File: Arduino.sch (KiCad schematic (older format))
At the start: 0 parts

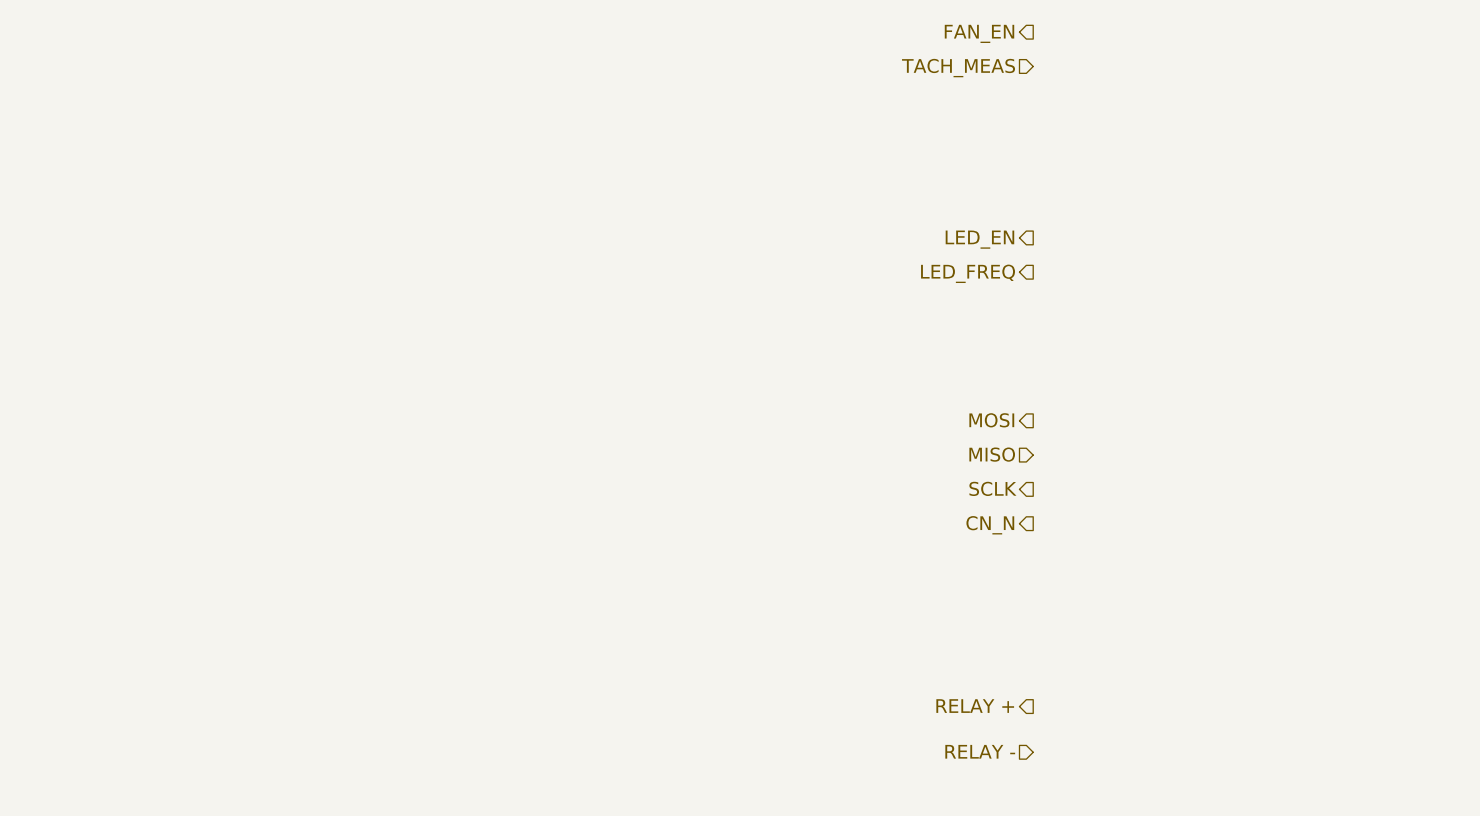
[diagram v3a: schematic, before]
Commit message: Completed Arduino Block Diagram and Fan Redesign
The commits as of this are now up to date with the videos released for
Contextual Electronics, Week 3.
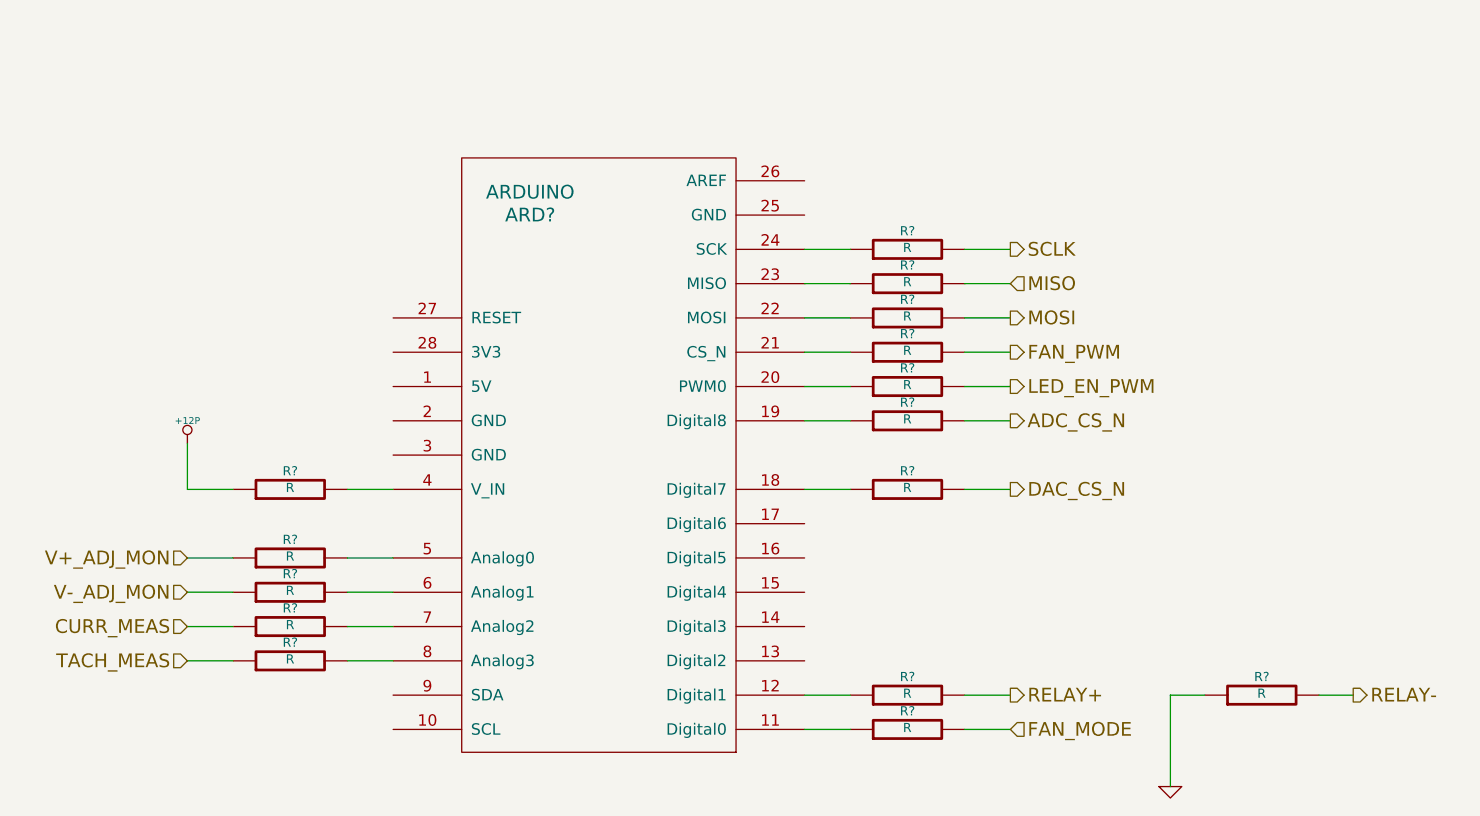
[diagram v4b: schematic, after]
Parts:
- added ARD?: ARDUINO, ~, symbol ARDUINO
- added R? (x15): R, ~, symbol R
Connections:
- net MISO: now also R?.2
- net MOSI: now also R?.2
- net SCLK: now also R?.2
- net TACH_MEAS: now also R?.1
- new net: ARD?.11 (Digital0), R?.1
- new net: ARD?.12 (Digital1), R?.1
- new net: ARD?.18 (Digital7), R?.1
- new net: ARD?.19 (Digital8), R?.1
- new net: ARD?.20 (PWM0), R?.1
- new net: ARD?.21 (CS_N), R?.1
- new net: ARD?.22 (MOSI), R?.1
- new net: ARD?.23 (MISO), R?.1
- new net: ARD?.24 (SCK), R?.1
- new net: ARD?.4 (V_IN), R?.2
- new net: ARD?.5 (Analog0), R?.2
- new net: ARD?.6 (Analog1), R?.2
- new net: ARD?.7 (Analog2), R?.2
- new net: ARD?.8 (Analog3), R?.2
- new net +12P: R?.1
- new net ADC_CS_N: R?.2
- new net CURR_MEAS: R?.1
- new net DAC_CS_N: R?.2
- new net FAN_MODE: R?.2
- new net FAN_PWM: R?.2
- new net GND: R?.1
- new net LED_EN_PWM: R?.2
- new net RELAY+: R?.2
- new net RELAY-: R?.2
- new net V+_ADJ_MON: R?.1
- new net V-_ADJ_MON: R?.1

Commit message: Initial layout of relay and thermocouple
All block diagrams completed through Week 3.  Component selection
spreadsheets created: Bench Buddy Session 1CE.xlsx = official part
selection and bom.xlsx is the version I came up with.

Part association and initial layout of the Relay and Thermocouple
sections completed.
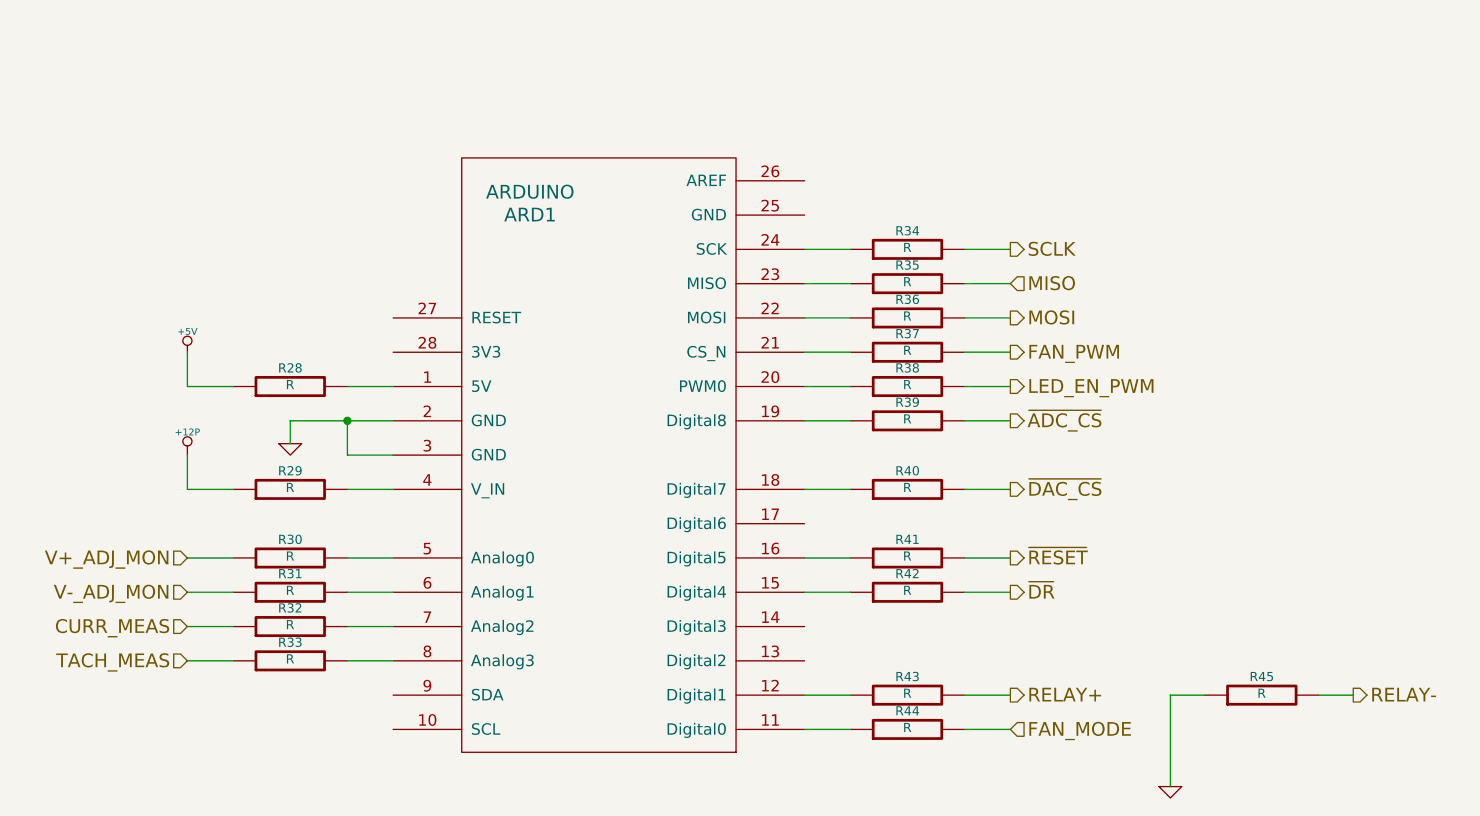
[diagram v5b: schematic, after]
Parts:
- added R28, R41, R42: R, ~, symbol R
- gave numbers to parts that had none: 16
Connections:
- net GND: now also ARD1.2 (GND), ARD1.3 (GND)
- net at ARD1.1 (5V): now also R28.2
- net at ARD1.15 (Digital4): now also R42.1
- net at ARD1.16 (Digital5): now also R41.1
- net ADC_CS_N renamed ~ADC_CS
- net DAC_CS_N renamed ~DAC_CS
- new net +5V: R28.1
- new net ~DR: R42.2
- new net ~RESET: R41.2
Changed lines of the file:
@@
 Sheet 9 9
 Title ""
-Date "6 feb 2014"
+Date "21 feb 2014"
 Rev ""
 Comp ""
@@
 SCLK
 Text HLabel 7900 4300 2    60   Output ~ 0
-DAC_CS_N
+~DAC_CS
 Text HLabel 7900 3850 2    60   Output ~ 0
 LED_EN_PWM
@@
 TACH_MEAS
 $Comp
-L ARDUINO ARD?
+L ARDUINO ARD1
 U 1 1 52F3CC17
 P 6100 4150
-F 0 "ARD?" H 5800 5200 60  0000 C CNN
+F 0 "ARD1" H 5800 5200 60  0000 C CNN
 F 1 "ARDUINO" H 5800 5300 60  0000 C CNN
 F 2 "~" H 6150 3600 60  0000 C CNN
@@
 	5200 4900 5000 4900
 $Comp
-L R R?
+L R R37
 U 1 1 52F3EA88
 P 7450 3700
-F 0 "R?" V 7530 3700 40  0000 C CNN
+F 0 "R37" V 7530 3700 40  0000 C CNN
 F 1 "R" V 7457 3701 40  0000 C CNN
 F 2 "~" V 7380 3700 30  0000 C CNN
@@
 	7700 3700 7900 3700
 $Comp
-L R R?
+L R R43
 U 1 1 52F3EAA6
 P 7450 5200
-F 0 "R?" V 7530 5200 40  0000 C CNN
+F 0 "R43" V 7530 5200 40  0000 C CNN
 F 1 "R" V 7457 5201 40  0000 C CNN
 F 2 "~" V 7380 5200 30  0000 C CNN
@@
 	7200 5200 7000 5200
 $Comp
-L GND #PWR?
+L GND #PWR056
 U 1 1 52F3F486
 P 8600 5600
-F 0 "#PWR?" H 8600 5600 30  0001 C CNN
+F 0 "#PWR056" H 8600 5600 30  0001 C CNN
 F 1 "GND" H 8600 5530 30  0001 C CNN
 F 2 "" H 8600 5600 60  0000 C CNN
@@
 	7900 5200 7700 5200
 $Comp
-L R R?
+L R R33
 U 1 1 52F3F4AB
 P 4750 5050
-F 0 "R?" V 4830 5050 40  0000 C CNN
+F 0 "R33" V 4830 5050 40  0000 C CNN
 F 1 "R" V 4757 5051 40  0000 C CNN
 F 2 "~" V 4680 5050 30  0000 C CNN
@@
 $EndComp
 $Comp
-L R R?
+L R R32
 U 1 1 52F3F4BB
 P 4750 4900
-F 0 "R?" V 4830 4900 40  0000 C CNN
+F 0 "R32" V 4830 4900 40  0000 C CNN
 F 1 "R" V 4757 4901 40  0000 C CNN
 F 2 "~" V 4680 4900 30  0000 C CNN
@@
 V-_ADJ_MON
 $Comp
-L R R?
+L R R31
 U 1 1 52F3F4E4
 P 4750 4750
-F 0 "R?" V 4830 4750 40  0000 C CNN
+F 0 "R31" V 4830 4750 40  0000 C CNN
 F 1 "R" V 4757 4751 40  0000 C CNN
 F 2 "~" V 4680 4750 30  0000 C CNN
@@
 $EndComp
 $Comp
-L R R?
+L R R30
 U 1 1 52F3F4EA
 P 4750 4600
-F 0 "R?" V 4830 4600 40  0000 C CNN
+F 0 "R30" V 4830 4600 40  0000 C CNN
 F 1 "R" V 4757 4601 40  0000 C CNN
 F 2 "~" V 4680 4600 30  0000 C CNN
@@
 	5200 4750 5000 4750
 $Comp
-L R R?
+L R R40
 U 1 1 52F3F532
 P 7450 4300
-F 0 "R?" V 7530 4300 40  0000 C CNN
+F 0 "R40" V 7530 4300 40  0000 C CNN
 F 1 "R" V 7457 4301 40  0000 C CNN
 F 2 "~" V 7380 4300 30  0000 C CNN
@@
 $EndComp
 $Comp
-L R R?
+L R R36
 U 1 1 52F3F538
 P 7450 3550
-F 0 "R?" V 7530 3550 40  0000 C CNN
+F 0 "R36" V 7530 3550 40  0000 C CNN
 F 1 "R" V 7457 3551 40  0000 C CNN
 F 2 "~" V 7380 3550 30  0000 C CNN
@@
 $EndComp
 $Comp
-L R R?
+L R R35
 U 1 1 52F3F53E
 P 7450 3400
-F 0 "R?" V 7530 3400 40  0000 C CNN
+F 0 "R35" V 7530 3400 40  0000 C CNN
 F 1 "R" V 7457 3401 40  0000 C CNN
 F 2 "~" V 7380 3400 30  0000 C CNN
@@
 $EndComp
 $Comp
-L R R?
+L R R34
 U 1 1 52F3F544
 P 7450 3250
-F 0 "R?" V 7530 3250 40  0000 C CNN
+F 0 "R34" V 7530 3250 40  0000 C CNN
 F 1 "R" V 7457 3251 40  0000 C CNN
 F 2 "~" V 7380 3250 30  0000 C CNN
@@
 	7200 4300 7000 4300
 $Comp
-L R R?
+L R R45
 U 1 1 52F3F59C
 P 9000 5200
-F 0 "R?" V 9080 5200 40  0000 C CNN
+F 0 "R45" V 9080 5200 40  0000 C CNN
 F 1 "R" V 9007 5201 40  0000 C CNN
 F 2 "~" V 8930 5200 30  0000 C CNN
@@
 	7700 3850 7900 3850
 $Comp
-L R R?
+L R R38
 U 1 1 52F3F5E7
 P 7450 3850
-F 0 "R?" V 7530 3850 40  0000 C CNN
+F 0 "R38" V 7530 3850 40  0000 C CNN
 F 1 "R" V 7457 3851 40  0000 C CNN
 F 2 "~" V 7380 3850 30  0000 C CNN
@@
 	7200 3850 7000 3850
 Text HLabel 7900 4000 2    60   Output ~ 0
-ADC_CS_N
+~ADC_CS
 Wire Wire Line
 	7700 4000 7900 4000
 $Comp
-L R R?
+L R R39
 U 1 1 52F47FE6
 P 7450 4000
-F 0 "R?" V 7530 4000 40  0000 C CNN
+F 0 "R39" V 7530 4000 40  0000 C CNN
 F 1 "R" V 7457 4001 40  0000 C CNN
 F 2 "~" V 7380 4000 30  0000 C CNN
@@
 	7700 5350 7900 5350
 $Comp
-L R R?
+L R R44
 U 1 1 52F41957
 P 7450 5350
-F 0 "R?" V 7530 5350 40  0000 C CNN
+F 0 "R44" V 7530 5350 40  0000 C CNN
 F 1 "R" V 7457 5351 40  0000 C CNN
 F 2 "~" V 7380 5350 30  0000 C CNN
@@
 	7200 5350 7000 5350
 $Comp
-L R R?
+L R R29
 U 1 1 52F42414
 P 4750 4300
-F 0 "R?" V 4830 4300 40  0000 C CNN
+F 0 "R29" V 4830 4300 40  0000 C CNN
 F 1 "R" V 4757 4301 40  0000 C CNN
 F 2 "~" V 4680 4300 30  0000 C CNN
@@
 	5000 4300 5200 4300
 $Comp
-L +12P #PWR?
+L +12P #PWR057
 U 1 1 52F4241E
-P 4300 4100
-F 0 "#PWR?" H 4300 4070 30  0001 C CNN
-F 1 "+12P" H 4300 4200 30  0000 C CNN
-F 2 "" H 4300 4100 60  0000 C CNN
-F 3 "" H 4300 4100 60  0000 C CNN
-	1    4300 4100
-	1    0    0    -1
-$EndComp
-Wire Wire Line
-	4300 4300 4300 4100
+P 4300 4150
+F 0 "#PWR057" H 4300 4120 30  0001 C CNN
+F 1 "+12P" H 4300 4250 30  0000 C CNN
+F 2 "" H 4300 4150 60  0000 C CNN
+F 3 "" H 4300 4150 60  0000 C CNN
+	1    4300 4150
+	1    0    0    -1
+$EndComp
+Wire Wire Line
+	4300 4300 4300 4150
+$Comp
+L R R28
+U 1 1 53010A6D
+P 4750 3850
+F 0 "R28" V 4830 3850 40  0000 C CNN
+F 1 "R" V 4757 3851 40  0000 C CNN
+F 2 "~" V 4680 3850 30  0000 C CNN
+F 3 "~" H 4750 3850 30  0000 C CNN
+	1    4750 3850
+	0    -1   -1   0
+$EndComp
+Wire Wire Line
+	4500 3850 4300 3850
+Wire Wire Line
+	5000 3850 5200 3850
+Wire Wire Line
+	4300 3850 4300 3700
+$Comp
+L +5V #PWR058
+U 1 1 53010A7E
+P 4300 3700
+F 0 "#PWR058" H 4300 3790 20  0001 C CNN
+F 1 "+5V" H 4300 3790 30  0000 C CNN
+F 2 "~" H 4300 3700 60  0000 C CNN
+F 3 "~" H 4300 3700 60  0000 C CNN
+	1    4300 3700
+	1    0    0    -1
+$EndComp
+$Comp
+L GND #PWR059
+U 1 1 53010A97
+P 4750 4100
+F 0 "#PWR059" H 4750 4100 30  0001 C CNN
+F 1 "GND" H 4750 4030 30  0001 C CNN
+F 2 "~" H 4750 4100 60  0000 C CNN
+F 3 "~" H 4750 4100 60  0000 C CNN
+	1    4750 4100
+	1    0    0    -1
+$EndComp
+Wire Wire Line
+	5200 4000 4750 4000
+Wire Wire Line
+	4750 4000 4750 4100
+Wire Wire Line
+	5200 4150 5000 4150
+Wire Wire Line
+	5000 4150 5000 4000
+Connection ~ 5000 4000
+Text HLabel 7900 4600 2    60   Output ~ 0
+~RESET
+Wire Wire Line
+	7700 4600 7900 4600
+$Comp
+L R R41
+U 1 1 53071A5A
+P 7450 4600
+F 0 "R41" V 7530 4600 40  0000 C CNN
+F 1 "R" V 7457 4601 40  0000 C CNN
+F 2 "~" V 7380 4600 30  0000 C CNN
+F 3 "~" H 7450 4600 30  0000 C CNN
+	1    7450 4600
+	0    -1   -1   0
+$EndComp
+Wire Wire Line
+	7200 4600 7000 4600
+Text HLabel 7900 4750 2    60   Output ~ 0
+~DR
+Wire Wire Line
+	7700 4750 7900 4750
+$Comp
+L R R42
+U 1 1 53071A63
+P 7450 4750
+F 0 "R42" V 7530 4750 40  0000 C CNN
+F 1 "R" V 7457 4751 40  0000 C CNN
+F 2 "~" V 7380 4750 30  0000 C CNN
+F 3 "~" H 7450 4750 30  0000 C CNN
+	1    7450 4750
+	0    -1   -1   0
+$EndComp
+Wire Wire Line
+	7200 4750 7000 4750
 $EndSCHEMATC
